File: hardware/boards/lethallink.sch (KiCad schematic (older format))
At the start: 5 parts, among them J1 PCIe-x4

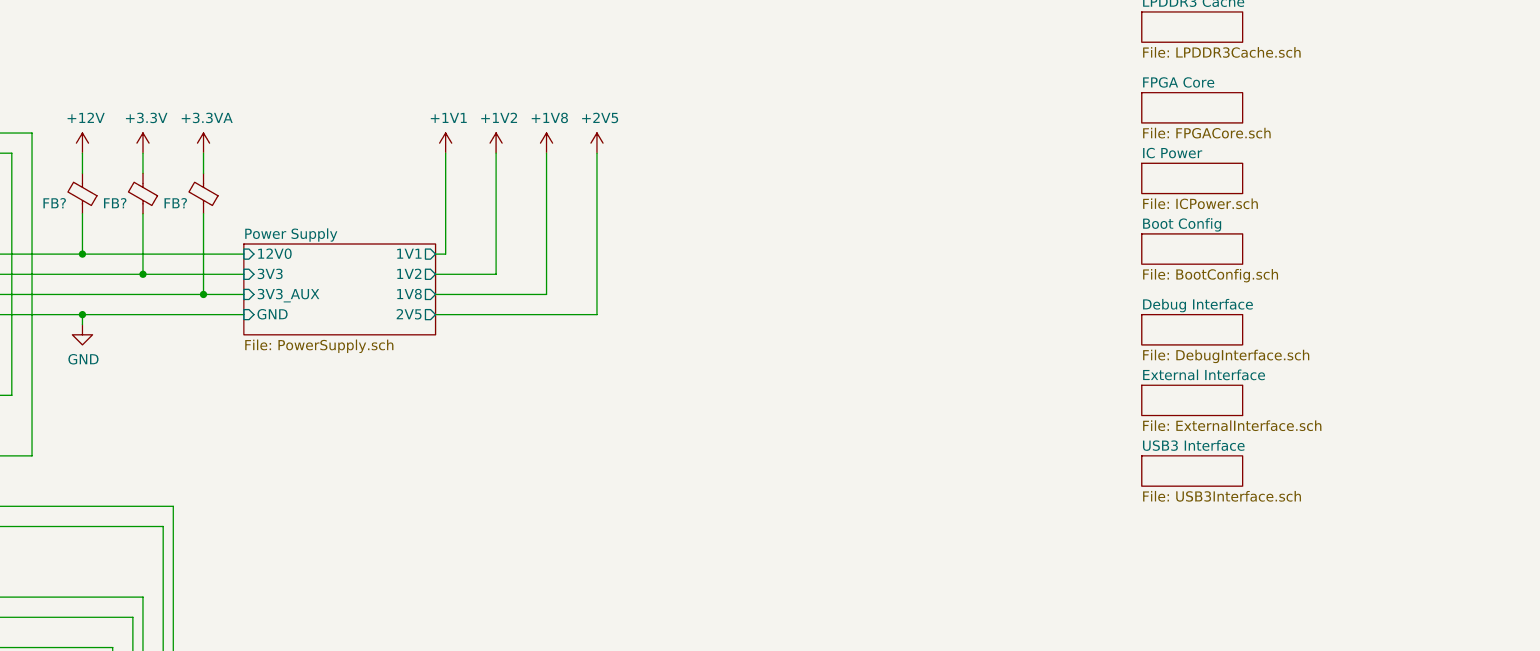
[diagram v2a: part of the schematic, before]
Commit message: Updated part mfr and added the proper part numbers
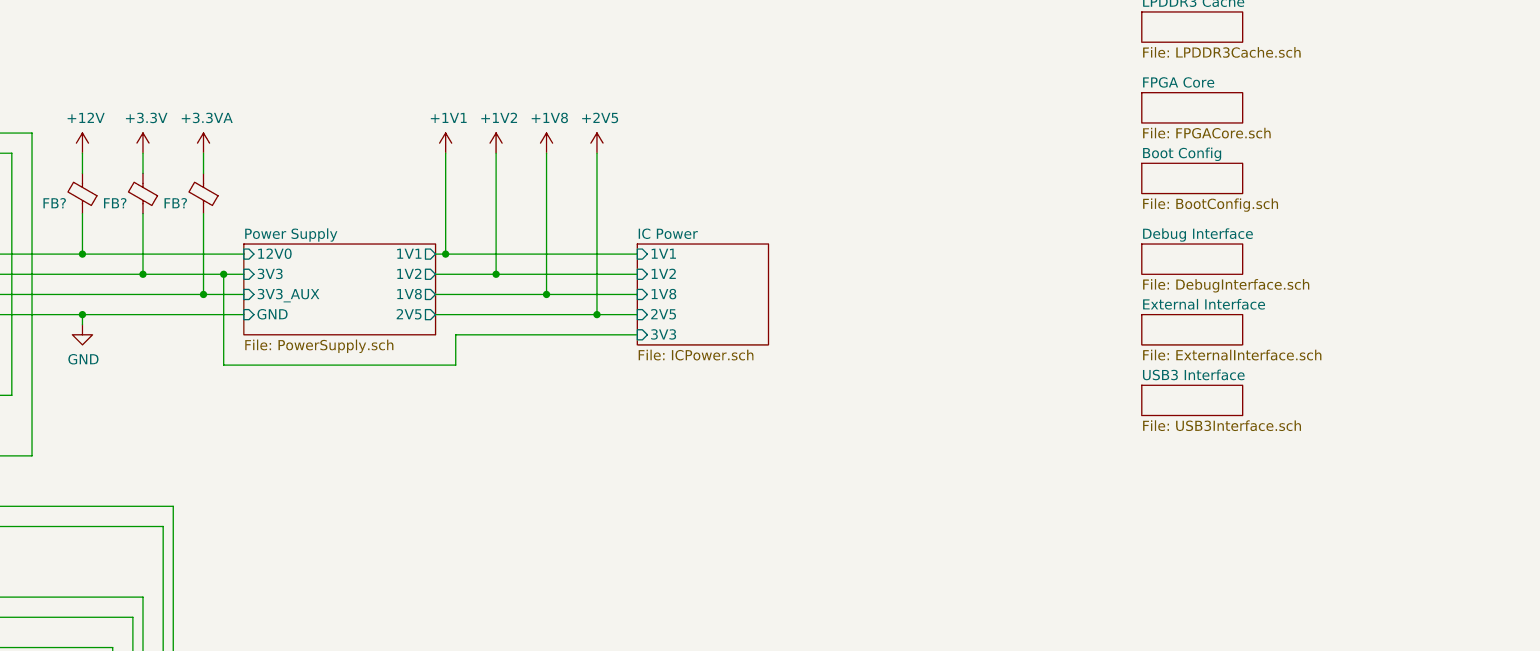
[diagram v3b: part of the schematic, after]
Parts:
- U?: MFR (none) -> Lattice; MPN (none) -> LFE5UM5G-85F-8BG381I
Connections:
- net Power Supply/3V3 renamed IC Power/3V3
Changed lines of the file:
@@
 Connection ~ 5200 1900
 Wire Wire Line
-	5200 1900 5700 1900
+	5200 1900 5600 1900
 $Sheet
-S 10150 1700 500  150
+S 10150 1350 500  150
 U 5EF66251
 F0 "Boot Config" 50
@@
 $EndSheet
 $Sheet
-S 10150 2100 500  150
+S 10150 1750 500  150
 U 5EF67D90
 F0 "Debug Interface" 50
@@
 $EndSheet
 $Sheet
-S 10150 2450 500  150
+S 10150 2100 500  150
 U 5EF6A128
 F0 "External Interface" 50
@@
 F 2 "" H 12850 150 50  0001 C CNN
 F 3 "" H 12850 150 50  0001 C CNN
+F 4 "Lattice" H 14200 0   50  0001 C CNN "MFR"
+F 5 "LFE5UM5G-85F-8BG381I" H 14200 0   50  0001 C CNN "MPN"
 	2    14200 0
 	1    0    0    -1
 $EndComp
 $Sheet
-S 10150 2800 500  150
+S 10150 2450 500  150
 U 5F2CAFD2
 F0 "USB3 Interface" 50
@@
 $EndSheet
 $Sheet
-S 10150 1350 500  150
+S 7650 1750 650  500
 U 5EF66188
 F0 "IC Power" 50
 F1 "ICPower.sch" 50
+F2 "3V3" I L 7650 2200 50
+F3 "1V1" I L 7650 1800 50
+F4 "1V8" I L 7650 2000 50
+F5 "2V5" I L 7650 2100 50
+F6 "1V2" I L 7650 1900 50
 $EndSheet
+Wire Wire Line
+	6700 1800 7650 1800
+Connection ~ 6700 1800
+Wire Wire Line
+	6950 1900 7650 1900
+Connection ~ 6950 1900
+Wire Wire Line
+	7200 2000 7650 2000
+Connection ~ 7200 2000
+Wire Wire Line
+	7450 2100 7650 2100
+Connection ~ 7450 2100
+Wire Wire Line
+	5600 1900 5600 2350
+Wire Wire Line
+	5600 2350 6750 2350
+Wire Wire Line
+	6750 2350 6750 2200
+Wire Wire Line
+	6750 2200 7650 2200
+Connection ~ 5600 1900
+Wire Wire Line
+	5600 1900 5700 1900
 $EndSCHEMATC

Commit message: Did some annotation and fixed the FPGA bank that was accidentally labled as the cypress part
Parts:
- U1: renamed from U?; footprint (none) -> lethalbit:318caBGA
- gave numbers to parts that had none: 3
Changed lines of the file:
@@
 	6650 1800 6700 1800
 $Comp
-L power:+1V1 #PWR?
+L power:+1V1 #PWR0105
 U 1 1 5EE6334E
 P 6700 1300
-F 0 "#PWR?" H 6700 1150 50  0001 C CNN
+F 0 "#PWR0105" H 6700 1150 50  0001 C CNN
 F 1 "+1V1" H 6715 1473 50  0000 C CNN
 F 2 "" H 6700 1300 50  0001 C CNN
@@
 P 6950 1300
 AR Path="/5EDF9F51/5EE1288F" Ref="#PWR?"  Part="1"
-AR Path="/5EE1288F" Ref="#PWR?"  Part="1"
-F 0 "#PWR?" H 6950 1150 50  0001 C CNN
+AR Path="/5EE1288F" Ref="#PWR0106"  Part="1"
+F 0 "#PWR0106" H 6950 1150 50  0001 C CNN
 F 1 "+1V2" H 6965 1473 50  0000 C CNN
 F 2 "" H 6950 1300 50  0001 C CNN
@@
 P 7200 1300
 AR Path="/5EDF9F51/5EE12889" Ref="#PWR?"  Part="1"
-AR Path="/5EE12889" Ref="#PWR?"  Part="1"
-F 0 "#PWR?" H 7200 1150 50  0001 C CNN
+AR Path="/5EE12889" Ref="#PWR0107"  Part="1"
+F 0 "#PWR0107" H 7200 1150 50  0001 C CNN
 F 1 "+1V8" H 7215 1473 50  0000 C CNN
 F 2 "" H 7200 1300 50  0001 C CNN
@@
 P 7450 1300
 AR Path="/5EDF9F51/5EE12883" Ref="#PWR?"  Part="1"
-AR Path="/5EE12883" Ref="#PWR?"  Part="1"
-F 0 "#PWR?" H 7450 1150 50  0001 C CNN
+AR Path="/5EE12883" Ref="#PWR0108"  Part="1"
+F 0 "#PWR0108" H 7450 1150 50  0001 C CNN
 F 1 "+2V5" H 7465 1473 50  0000 C CNN
 F 2 "" H 7450 1300 50  0001 C CNN
@@
 	4300 1900 5200 1900
 $Comp
-L Device:Ferrite_Bead_Small FB?
+L Device:Ferrite_Bead_Small FB1
 U 1 1 5EEA5842
 P 4900 1500
-F 0 "FB?" H 5100 1550 50  0000 R CNN
+F 0 "FB1" H 5100 1550 50  0000 R CNN
 F 1 "Ferrite_Bead_Small" H 5050 1700 50  0001 R CNN
 F 2 "" V 4830 1500 50  0001 C CNN
@@
 $EndComp
 $Comp
-L Device:Ferrite_Bead_Small FB?
+L Device:Ferrite_Bead_Small FB2
 U 1 1 5EEA7C39
 P 5200 1500
-F 0 "FB?" H 5400 1550 50  0000 R CNN
+F 0 "FB2" H 5400 1550 50  0000 R CNN
 F 1 "Ferrite_Bead_Small" H 5350 1700 50  0001 R CNN
 F 2 "" V 5130 1500 50  0001 C CNN
@@
 $EndComp
 $Comp
-L Device:Ferrite_Bead_Small FB?
+L Device:Ferrite_Bead_Small FB3
 U 1 1 5EEAB060
 P 5500 1500
-F 0 "FB?" H 5700 1550 50  0000 R CNN
+F 0 "FB3" H 5700 1550 50  0000 R CNN
 F 1 "Ferrite_Bead_Small" H 5650 1700 50  0001 R CNN
 F 2 "" V 5430 1500 50  0001 C CNN
@@
 $EndSheet
 $Comp
-L lethalbit:ECP5UM5G-381caBGA U?
+L lethalbit:ECP5UM5G-381caBGA U1
 U 2 1 5EF7DF2B
 P 14200 0
-F 0 "U?" H 14200 348 50  0000 C CNN
+F 0 "U1" H 14200 348 50  0000 C CNN
 F 1 "ECP5UM5G-381caBGA" H 14200 257 50  0000 C CNN
-F 2 "" H 12850 150 50  0001 C CNN
+F 2 "lethalbit:318caBGA" H 12850 150 50  0001 C CNN
 F 3 "" H 12850 150 50  0001 C CNN
 F 4 "Lattice" H 14200 0   50  0001 C CNN "MFR"

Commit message: Some more mist schematic edits
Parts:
- removed U1: ECP5UM5G-381caBGA, lethalbit:318caBGA, symbol lethalbit:ECP5UM5G-381caBGA
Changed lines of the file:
@@
 F1 "LPDDR3Cache.sch" 50
-$EndSheet
-$Sheet
-S 10150 1000 500  150
-U 5EDF8786
-F0 "FPGA Core" 50
-F1 "FPGACore.sch" 50
 $EndSheet
 Wire Wire Line
@@
 	5200 1900 5600 1900
 $Sheet
-S 10150 1350 500  150
-U 5EF66251
-F0 "Boot Config" 50
-F1 "BootConfig.sch" 50
-$EndSheet
-$Sheet
-S 10150 1750 500  150
-U 5EF67D90
-F0 "Debug Interface" 50
-F1 "DebugInterface.sch" 50
-$EndSheet
-$Sheet
-S 10150 2100 500  150
-U 5EF6A128
-F0 "External Interface" 50
-F1 "ExternalInterface.sch" 50
-$EndSheet
-$Comp
-L lethalbit:ECP5UM5G-381caBGA U1
-U 2 1 5EF7DF2B
-P 14200 0
-F 0 "U1" H 14200 348 50  0000 C CNN
-F 1 "ECP5UM5G-381caBGA" H 14200 257 50  0000 C CNN
-F 2 "lethalbit:318caBGA" H 12850 150 50  0001 C CNN
-F 3 "" H 12850 150 50  0001 C CNN
-F 4 "Lattice" H 14200 0   50  0001 C CNN "MFR"
-F 5 "LFE5UM5G-85F-8BG381I" H 14200 0   50  0001 C CNN "MPN"
-	2    14200 0
-	1    0    0    -1
-$EndComp
-$Sheet
-S 10150 2450 500  150
-U 5F2CAFD2
-F0 "USB3 Interface" 50
-F1 "USB3Interface.sch" 50
-$EndSheet
-$Sheet
 S 7650 1750 650  500
 U 5EF66188
@@
 Wire Wire Line
 	5600 1900 5700 1900
+$Sheet
+S 10150 2100 500  150
+U 5F2CAFD2
+F0 "USB3 Interface" 50
+F1 "USB3Interface.sch" 50
+$EndSheet
+$Sheet
+S 10150 1750 500  150
+U 5EF6A128
+F0 "External Interface" 50
+F1 "ExternalInterface.sch" 50
+$EndSheet
+$Sheet
+S 10150 1400 500  150
+U 5EF67D90
+F0 "Debug Interface" 50
+F1 "DebugInterface.sch" 50
+$EndSheet
+$Sheet
+S 10150 1000 500  150
+U 5EF66251
+F0 "Boot Config" 50
+F1 "BootConfig.sch" 50
+$EndSheet
 $EndSCHEMATC

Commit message: Lots of small updates, getting values specified for parts, switched the BJT to NFETs
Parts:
- FB1: value Ferrite_Bead_Small -> 100 @ 100MHz; footprint (none) -> Resistor_SMD:R_0603_1608Metric; MFR (none) -> Murata Electronics; MPN (none) -> BLM18KG101TN1D
- FB2, FB3: value Ferrite_Bead_Small -> 220 @ 100Mhz; footprint (none) -> Resistor_SMD:R_0603_1608Metric; MFR (none) -> Murata Electronics; MPN (none) -> BLM18AG221SN1D
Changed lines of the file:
@@
 $Descr A4 11693 8268
 encoding utf-8
-Sheet 1 11
+Sheet 1 10
 Title ""
 Date ""
@@
 Wire Wire Line
 	6650 1800 6700 1800
-$Comp
-L power:+1V1 #PWR0105
-U 1 1 5EE6334E
-P 6700 1300
-F 0 "#PWR0105" H 6700 1150 50  0001 C CNN
-F 1 "+1V1" H 6715 1473 50  0000 C CNN
-F 2 "" H 6700 1300 50  0001 C CNN
-F 3 "" H 6700 1300 50  0001 C CNN
-	1    6700 1300
-	1    0    0    -1
-$EndComp
 Wire Wire Line
 	7450 2100 6650 2100
@@
 F7 "2V5" O R 6650 2100 50
 F8 "1V8" O R 6650 2000 50
-F9 "1V1" O R 6650 1800 50
+F9 "1V5" O R 6650 1800 50
 $EndSheet
 Wire Wire Line
@@
 P 4900 1500
 F 0 "FB1" H 5100 1550 50  0000 R CNN
-F 1 "Ferrite_Bead_Small" H 5050 1700 50  0001 R CNN
-F 2 "" V 4830 1500 50  0001 C CNN
+F 1 "100 @ 100MHz" H 5050 1700 50  0001 R CNN
+F 2 "Resistor_SMD:R_0603_1608Metric" V 4830 1500 50  0001 C CNN
 F 3 "~" H 4900 1500 50  0001 C CNN
+F 4 "Murata Electronics" H 4900 1500 50  0001 C CNN "MFR"
+F 5 "BLM18KG101TN1D" H 4900 1500 50  0001 C CNN "MPN"
 	1    4900 1500
-	-1   0    0    1
-$EndComp
-$Comp
-L Device:Ferrite_Bead_Small FB2
-U 1 1 5EEA7C39
-P 5200 1500
-F 0 "FB2" H 5400 1550 50  0000 R CNN
-F 1 "Ferrite_Bead_Small" H 5350 1700 50  0001 R CNN
-F 2 "" V 5130 1500 50  0001 C CNN
-F 3 "~" H 5200 1500 50  0001 C CNN
-	1    5200 1500
-	-1   0    0    1
-$EndComp
-$Comp
-L Device:Ferrite_Bead_Small FB3
-U 1 1 5EEAB060
-P 5500 1500
-F 0 "FB3" H 5700 1550 50  0000 R CNN
-F 1 "Ferrite_Bead_Small" H 5650 1700 50  0001 R CNN
-F 2 "" V 5430 1500 50  0001 C CNN
-F 3 "~" H 5500 1500 50  0001 C CNN
-	1    5500 1500
 	-1   0    0    1
 $EndComp
@@
 F1 "ICPower.sch" 50
 F2 "3V3" I L 7650 2200 50
-F3 "1V1" I L 7650 1800 50
-F4 "1V8" I L 7650 2000 50
-F5 "2V5" I L 7650 2100 50
-F6 "1V2" I L 7650 1900 50
+F3 "1V8" I L 7650 2000 50
+F4 "2V5" I L 7650 2100 50
+F5 "1V2" I L 7650 1900 50
+F6 "1V5" I L 7650 1800 50
 $EndSheet
 Wire Wire Line
@@
 F1 "BootConfig.sch" 50
 $EndSheet
+$Comp
+L power:+1V5 #PWR0105
+U 1 1 5F022207
+P 6700 1300
+F 0 "#PWR0105" H 6700 1150 50  0001 C CNN
+F 1 "+1V5" H 6715 1473 50  0000 C CNN
+F 2 "" H 6700 1300 50  0001 C CNN
+F 3 "" H 6700 1300 50  0001 C CNN
+	1    6700 1300
+	1    0    0    -1
+$EndComp
+$Comp
+L Device:Ferrite_Bead_Small FB2
+U 1 1 5F579DEB
+P 5200 1500
+F 0 "FB2" H 5400 1550 50  0000 R CNN
+F 1 "220 @ 100Mhz" H 5350 1700 50  0001 R CNN
+F 2 "Resistor_SMD:R_0603_1608Metric" V 5130 1500 50  0001 C CNN
+F 3 "~" H 5200 1500 50  0001 C CNN
+F 4 "Murata Electronics" H 5200 1500 50  0001 C CNN "MFR"
+F 5 "BLM18AG221SN1D" H 5200 1500 50  0001 C CNN "MPN"
+	1    5200 1500
+	-1   0    0    1
+$EndComp
+$Comp
+L Device:Ferrite_Bead_Small FB3
+U 1 1 5F57A174
+P 5500 1500
+F 0 "FB3" H 5700 1550 50  0000 R CNN
+F 1 "220 @ 100Mhz" H 5650 1700 50  0001 R CNN
+F 2 "Resistor_SMD:R_0603_1608Metric" V 5430 1500 50  0001 C CNN
+F 3 "~" H 5500 1500 50  0001 C CNN
+F 4 "Murata Electronics" H 5500 1500 50  0001 C CNN "MFR"
+F 5 "BLM18AG221SN1D" H 5500 1500 50  0001 C CNN "MPN"
+	1    5500 1500
+	-1   0    0    1
+$EndComp
 $EndSCHEMATC

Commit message: Some strugglebusting on getting the ERC errors cleaned up a bit
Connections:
- net +3.3VA: now also FB3.1; no longer FB3.2
- net +3V3: now also FB2.1; no longer FB2.2
- net IC Power/3V3: no longer names the net of J1.A10 (3V3), J1.A9 (3V3), J1.B8 (3V3)
- net IC Power/3V3: now also FB2.2; no longer FB2.1
- net Power Supply/12V0: no longer names the net of FB1.1, J1.A2 (12V0), J1.A3 (12V0), J1.B1 (12V0), J1.B2 (12V0), J1.B3 (12V0)
- net Power Supply/3V3_AUX: no longer names the net of J1.B10 (3V3_AUX)
- net Power Supply/3V3_AUX: now also FB3.2; no longer FB3.1
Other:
- moved on the sheet: FB1, FB2, FB3
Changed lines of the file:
@@
 $EndComp
-Wire Wire Line
-	4900 1400 4900 1300
-Wire Wire Line
-	5200 1400 5200 1300
-Wire Wire Line
-	5500 1400 5500 1300
 Wire Wire Line
 	4300 2100 4900 2100
@@
 F9 "1V5" O R 6650 1800 50
 $EndSheet
-Wire Wire Line
-	4300 1800 4900 1800
-Wire Wire Line
-	4300 1900 5200 1900
 $Comp
 L Device:Ferrite_Bead_Small FB1
 U 1 1 5EEA5842
-P 4900 1500
-F 0 "FB1" H 5100 1550 50  0000 R CNN
-F 1 "100 @ 100MHz" H 5050 1700 50  0001 R CNN
-F 2 "Resistor_SMD:R_0603_1608Metric" V 4830 1500 50  0001 C CNN
-F 3 "~" H 4900 1500 50  0001 C CNN
-F 4 "Murata Electronics" H 4900 1500 50  0001 C CNN "MFR"
-F 5 "BLM18KG101TN1D" H 4900 1500 50  0001 C CNN "MPN"
-	1    4900 1500
-	-1   0    0    1
-$EndComp
-Wire Wire Line
-	5500 1600 5500 2000
-Connection ~ 5500 2000
-Wire Wire Line
-	5500 2000 5700 2000
+P 4800 1800
+F 0 "FB1" H 5000 1850 50  0000 R CNN
+F 1 "100 @ 100MHz" H 4950 2000 50  0001 R CNN
+F 2 "Resistor_SMD:R_0603_1608Metric" V 4730 1800 50  0001 C CNN
+F 3 "~" H 4800 1800 50  0001 C CNN
+F 4 "Murata Electronics" H 4800 1800 50  0001 C CNN "MFR"
+F 5 "BLM18KG101TN1D" H 4800 1800 50  0001 C CNN "MPN"
+	1    4800 1800
+	0    -1   -1   0
+$EndComp
 Connection ~ 4900 2100
-Wire Wire Line
-	4900 2100 5700 2100
-Wire Wire Line
-	4300 2000 5500 2000
-Wire Wire Line
-	4900 1600 4900 1800
-Connection ~ 4900 1800
-Wire Wire Line
-	4900 1800 5700 1800
-Wire Wire Line
-	5200 1600 5200 1900
-Connection ~ 5200 1900
-Wire Wire Line
-	5200 1900 5600 1900
 Wire Wire Line
 	6700 1800 7650 1800
@@
 L Device:Ferrite_Bead_Small FB2
 U 1 1 5F579DEB
-P 5200 1500
-F 0 "FB2" H 5400 1550 50  0000 R CNN
-F 1 "220 @ 100Mhz" H 5350 1700 50  0001 R CNN
-F 2 "Resistor_SMD:R_0603_1608Metric" V 5130 1500 50  0001 C CNN
-F 3 "~" H 5200 1500 50  0001 C CNN
-F 4 "Murata Electronics" H 5200 1500 50  0001 C CNN "MFR"
-F 5 "BLM18AG221SN1D" H 5200 1500 50  0001 C CNN "MPN"
-	1    5200 1500
-	-1   0    0    1
+P 5100 1900
+F 0 "FB2" H 5050 1850 50  0000 R CNN
+F 1 "220 @ 100Mhz" H 5250 2100 50  0001 R CNN
+F 2 "Resistor_SMD:R_0603_1608Metric" V 5030 1900 50  0001 C CNN
+F 3 "~" H 5100 1900 50  0001 C CNN
+F 4 "Murata Electronics" H 5100 1900 50  0001 C CNN "MFR"
+F 5 "BLM18AG221SN1D" H 5100 1900 50  0001 C CNN "MPN"
+	1    5100 1900
+	0    1    1    0
 $EndComp
 $Comp
 L Device:Ferrite_Bead_Small FB3
 U 1 1 5F57A174
-P 5500 1500
-F 0 "FB3" H 5700 1550 50  0000 R CNN
-F 1 "220 @ 100Mhz" H 5650 1700 50  0001 R CNN
-F 2 "Resistor_SMD:R_0603_1608Metric" V 5430 1500 50  0001 C CNN
-F 3 "~" H 5500 1500 50  0001 C CNN
-F 4 "Murata Electronics" H 5500 1500 50  0001 C CNN "MFR"
-F 5 "BLM18AG221SN1D" H 5500 1500 50  0001 C CNN "MPN"
-	1    5500 1500
-	-1   0    0    1
+P 5400 2000
+F 0 "FB3" H 5350 1950 50  0000 R CNN
+F 1 "220 @ 100Mhz" H 5550 2200 50  0001 R CNN
+F 2 "Resistor_SMD:R_0603_1608Metric" V 5330 2000 50  0001 C CNN
+F 3 "~" H 5400 2000 50  0001 C CNN
+F 4 "Murata Electronics" H 5400 2000 50  0001 C CNN "MFR"
+F 5 "BLM18AG221SN1D" H 5400 2000 50  0001 C CNN "MPN"
+	1    5400 2000
+	0    1    1    0
 $EndComp
 $Sheet
@@
 F6 "1V5" I L 7650 1800 50
 $EndSheet
+Wire Wire Line
+	4300 1800 4700 1800
+Wire Wire Line
+	4300 1900 5000 1900
+Wire Wire Line
+	5500 2000 5700 2000
+Wire Wire Line
+	4900 1300 4900 1800
+Connection ~ 4900 1800
+Wire Wire Line
+	5200 1300 5200 1900
+Wire Wire Line
+	5500 1300 5500 2000
+Connection ~ 5200 1900
+Wire Wire Line
+	4300 2000 5300 2000
+Wire Wire Line
+	4900 1800 5700 1800
+Connection ~ 5500 2000
+Wire Wire Line
+	4900 2100 5700 2100
+Wire Wire Line
+	5200 1900 5600 1900
 $EndSCHEMATC
